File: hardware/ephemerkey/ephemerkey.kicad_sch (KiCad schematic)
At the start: 0 parts

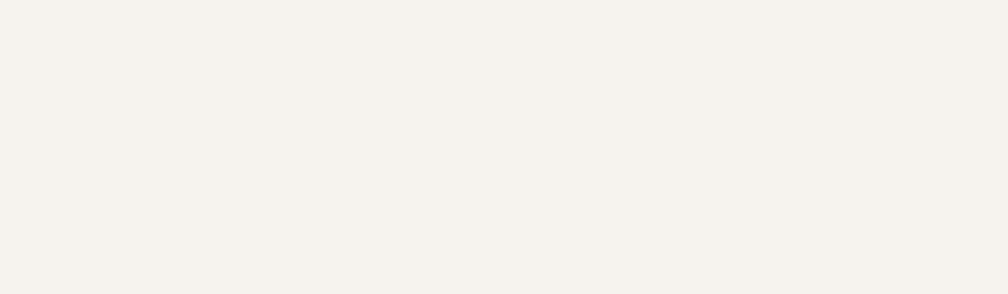
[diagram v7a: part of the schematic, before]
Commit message: hardware: add optional ESP32-C3 WiFi + audit-log EEPROM (wifi/storage sheets)
Two new generated sheets (existing sheets untouched, no force-regen):

WiFi (wifi.kicad_sch, optional — depopulate to omit):
- ESP32-C3-MINI-1-N4 (C2838502) on its own AP2112K-3.3 rail from VSYS, so
  350mA TX bursts never load the TPS63900 (400mA) or the GNSS VCC_RF rail
- 3 MCU pins total: PB5 = LDO EN (power cycle = reset; 100k default-off),
  PA2 = LPUART1_TX doubling as the IO9 boot strap, PA3 = LPUART1_RX
  (wake-from-Stop); accel INTs move PA2/PA3 -> PB3/PA8, zero spares remain
- USB-CDC bridge flashing plan (stock esptool.py through the STM32) and
  DNP 0R links to BOOT0/NRST for ESP-driven ROM recovery of a blank MCU
- vendored symbol/footprint/STEP from espressif/kicad-libraries (first
  entries in the project lib; bundled KiCad has no C3-MINI-1)

Storage (storage.kicad_sch):
- M24M02E-FMC6TG (C29549719) 2Mbit I2C EEPROM in UFDFPN8 2x3mm DFN at
  0x50-0x53 on I2C1 — zero new pins, 350nA standby, 4M-cycle endurance
- audit-log strategy in DESIGN.md: encrypted + HMAC-SHA1-chained 32B ring
  (~8000 records), secrets stay in internal flash (RDP/HDP), STM32 OTA
  images stage in the ESP32's 4MB flash over LPUART1
- footprint vendored from LCSC via easyeda2kicad and verified against the
  ST UFDFPN8 outline — KiCad's bundled DFN-8 2x3 is a different package
  (pad rows 1.88mm apart vs 3.0mm) and would not assemble

R17 was taken by a hand-added 4.7k on Sensors, so the WiFi LDO EN pulldown
is R26. check-ephemerkey: 89 components, 89/89 footprints, no dup refs.

Co-Authored-By: Claude Fable 5 <noreply@anthropic.com>
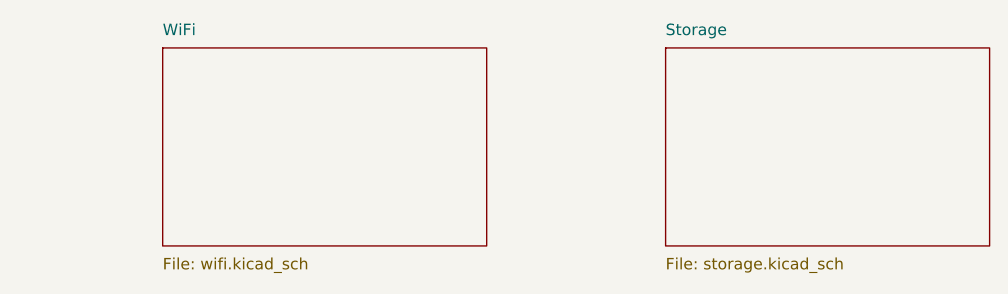
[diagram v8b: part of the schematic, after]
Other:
- added sheet Storage (storage.kicad_sch)
- added sheet WiFi (wifi.kicad_sch)
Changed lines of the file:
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@@
 	(sheet
 		(at 40.64 40.64)
-		(size 36.00 22.00)
-		(fields_autoplaced yes)
-		(stroke (width 0.1524) (type solid))
-		(fill (color 0 0 0 0.0000))
+		(size 36 22)
+		(exclude_from_sim no)
+		(in_bom yes)
+		(on_board yes)
+		(dnp no)
+		(fields_autoplaced yes)
+		(stroke
+			(width 0.1524)
+			(type solid)
+		)
+		(fill
+			(color 0 0 0 0)
+		)
 		(property "Sheetname" "MCU"
 			(at 40.64 39.37 0)
-			(effects (font (size 1.27 1.27)) (justify left bottom))
+			(show_name no)
+			(do_not_autoplace no)
+			(effects
+				(font
+					(size 1.27 1.27)
+				)
+				(justify left bottom)
+			)
 		)
 		(property "Sheetfile" "mcu.kicad_sch"
 			(at 40.64 63.91 0)
-			(effects (font (size 1.27 1.27)) (justify left top))
+			(show_name no)
+			(do_not_autoplace no)
+			(effects
+				(font
+					(size 1.27 1.27)
+				)
+				(justify left top)
+			)
 		)
 	)
 	(sheet
 		(at 96.52 40.64)
-		(size 36.00 22.00)
-		(fields_autoplaced yes)
-		(stroke (width 0.1524) (type solid))
-		(fill (color 0 0 0 0.0000))
+		(size 36 22)
+		(exclude_from_sim no)
+		(in_bom yes)
+		(on_board yes)
+		(dnp no)
+		(fields_autoplaced yes)
+		(stroke
+			(width 0.1524)
+			(type solid)
+		)
+		(fill
+			(color 0 0 0 0)
+		)
 		(property "Sheetname" "PSU"
 			(at 96.52 39.37 0)
-			(effects (font (size 1.27 1.27)) (justify left bottom))
+			(show_name no)
+			(do_not_autoplace no)
+			(effects
+				(font
+					(size 1.27 1.27)
+				)
+				(justify left bottom)
+			)
 		)
 		(property "Sheetfile" "psu.kicad_sch"
 			(at 96.52 63.91 0)
-			(effects (font (size 1.27 1.27)) (justify left top))
-		)
-	)
-	(sheet
-		(at 152.40 40.64)
-		(size 36.00 22.00)
-		(fields_autoplaced yes)
-		(stroke (width 0.1524) (type solid))
-		(fill (color 0 0 0 0.0000))
+			(show_name no)
+			(do_not_autoplace no)
+			(effects
+				(font
+					(size 1.27 1.27)
+				)
+				(justify left top)
+			)
+		)
+	)
+	(sheet
+		(at 152.4 40.64)
+		(size 36 22)
+		(exclude_from_sim no)
+		(in_bom yes)
+		(on_board yes)
+		(dnp no)
+		(fields_autoplaced yes)
+		(stroke
+			(width 0.1524)
+			(type solid)
+		)
+		(fill
+			(color 0 0 0 0)
+		)
 		(property "Sheetname" "GNSS"
-			(at 152.40 39.37 0)
-			(effects (font (size 1.27 1.27)) (justify left bottom))
+			(at 152.4 39.37 0)
+			(show_name no)
+			(do_not_autoplace no)
+			(effects
+				(font
+					(size 1.27 1.27)
+				)
+				(justify left bottom)
+			)
 		)
 		(property "Sheetfile" "gnss.kicad_sch"
-			(at 152.40 63.91 0)
-			(effects (font (size 1.27 1.27)) (justify left top))
+			(at 152.4 63.91 0)
+			(show_name no)
+			(do_not_autoplace no)
+			(effects
+				(font
+					(size 1.27 1.27)
+				)
+				(justify left top)
+			)
 		)
 	)
 	(sheet
 		(at 208.28 40.64)
-		(size 36.00 22.00)
-		(fields_autoplaced yes)
-		(stroke (width 0.1524) (type solid))
-		(fill (color 0 0 0 0.0000))
+		(size 36 22)
+		(exclude_from_sim no)
+		(in_bom yes)
+		(on_board yes)
+		(dnp no)
+		(fields_autoplaced yes)
+		(stroke
+			(width 0.1524)
+			(type solid)
+		)
+		(fill
+			(color 0 0 0 0)
+		)
 		(property "Sheetname" "Sensors"
 			(at 208.28 39.37 0)
-			(effects (font (size 1.27 1.27)) (justify left bottom))
+			(show_name no)
+			(do_not_autoplace no)
+			(effects
+				(font
+					(size 1.27 1.27)
+				)
+				(justify left bottom)
+			)
 		)
 		(property "Sheetfile" "sensors.kicad_sch"
 			(at 208.28 63.91 0)
-			(effects (font (size 1.27 1.27)) (justify left top))
-		)
-	)
+			(show_name no)
+			(do_not_autoplace no)
+			(effects
+				(font
+					(size 1.27 1.27)
+				)
+				(justify left top)
+			)
+		)
+	)
+	(sheet
+		(at 264.16 40.64)
+		(size 36 22)
+		(exclude_from_sim no)
+		(in_bom yes)
+		(on_board yes)
+		(dnp no)
+		(fields_autoplaced yes)
+		(stroke
+			(width 0.1524)
+			(type solid)
+		)
+		(fill
+			(color 0 0 0 0)
+		)
+		(property "Sheetname" "WiFi"
+			(at 264.16 39.37 0)
+			(show_name no)
+			(do_not_autoplace no)
+			(effects
+				(font
+					(size 1.27 1.27)
+				)
+				(justify left bottom)
+			)
+		)
+		(property "Sheetfile" "wifi.kicad_sch"
+			(at 264.16 63.91 0)
+			(show_name no)
+			(do_not_autoplace no)
+			(effects
+				(font
+					(size 1.27 1.27)
+				)
+				(justify left top)
+			)
+		)
+	)
+	(sheet
+		(at 320.04 40.64)
+		(size 36 22)
+		(exclude_from_sim no)
+		(in_bom yes)
+		(on_board yes)
+		(dnp no)
+		(fields_autoplaced yes)
+		(stroke
+			(width 0.1524)
+			(type solid)
+		)
+		(fill
+			(color 0 0 0 0)
+		)
+		(property "Sheetname" "Storage"
+			(at 320.04 39.37 0)
+			(show_name no)
+			(do_not_autoplace no)
+			(effects
+				(font
+					(size 1.27 1.27)
+				)
+				(justify left bottom)
+			)
+		)
+		(property "Sheetfile" "storage.kicad_sch"
+			(at 320.04 63.91 0)
+			(show_name no)
+			(do_not_autoplace no)
+			(effects
+				(font
+					(size 1.27 1.27)
+				)
+				(justify left top)
+			)
+		)
+	)
